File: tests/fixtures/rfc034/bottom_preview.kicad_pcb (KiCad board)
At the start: 2 copper layers, 75 x 58 mm, 16 parts, among them Q1 NPN_SOT23_BEC, Q2 NPN_SOT23_BEC, Q3 NPN_SOT23_BEC, Q4 NPN_SOT23_BEC, U1 W25Q128JV, U2 W25Q128JV, U3 W25Q128JV, U4 W25Q128JV

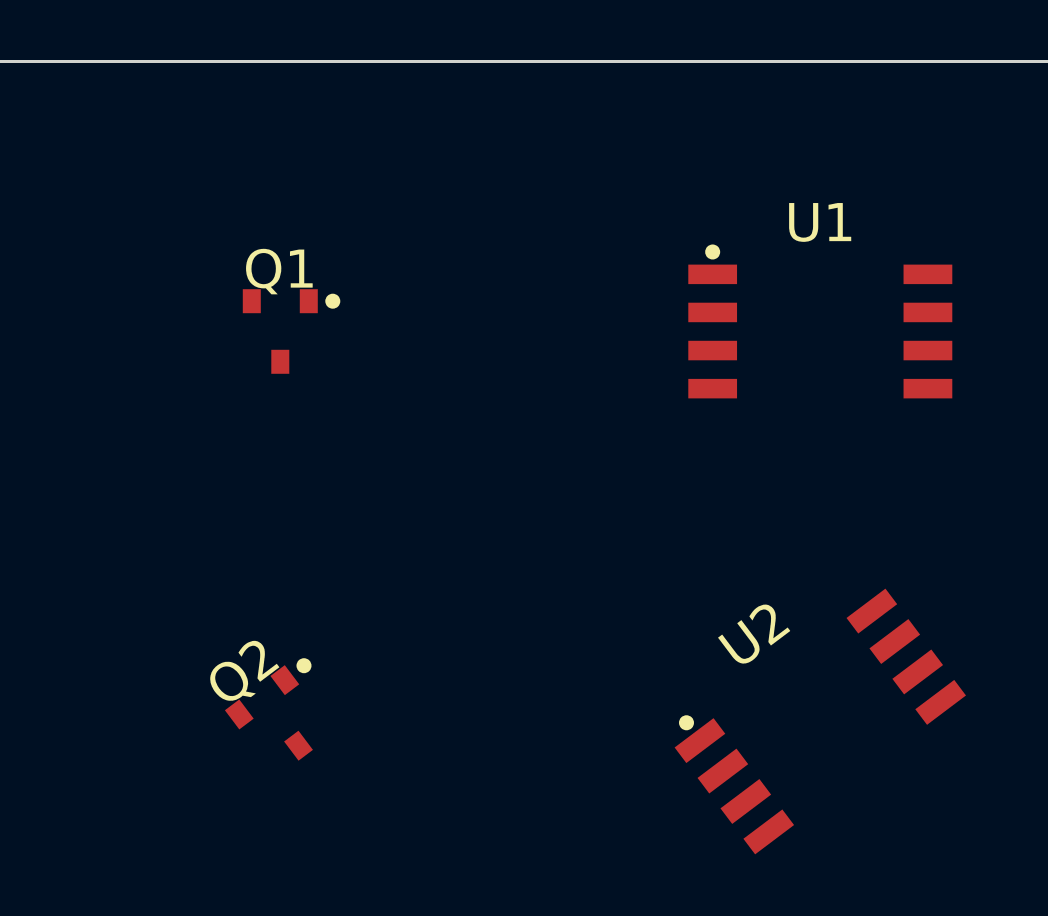
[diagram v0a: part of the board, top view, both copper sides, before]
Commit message: Move nine footprints onto the assembler's frame (library plan W3)
The C2 board 1 preview measured these footprints at a constant quarter
turn from the assembler's models, the same on every copy:

- transistor 0.2.0: FP_JSCJ_SOT23 by (0, 0, 90);
- soic 0.3.0: SOIC8P127X790X216N, TI_D0008A_4214825C,
  TSSOP24P65_TI_PW0024A, KICAD_SOIC_8_3_9X4_9MM_P1_27MM and
  KICAD_TSSOP_20_4_4X6_5MM_P0_65MM by (0, 0, 270);
- qfp 0.3.0: QFP50P900X900X160_48N, KICAD_LQFP_32_7X7MM_P0_8MM and
  KICAD_LQFP_48_7X7MM_P0_5MM by (0, 0, 270).

The hand-written ones are moved with tools/realign_footprint.py. The
generated ones are moved by gen_stm32_footprints.py from
tools/stm32_footprint_data/supplier_frames.json, which
tests/stm32_footprints.rs applies independently to the KiCad snapshot.

The change is breaking, so the three packages and every dependent
whose parts use a moved footprint take a minor version: can, flash,
@st/stm32, @ti/logic, @contrib/comparator, @wch/ch32 and
@gigadevice/gd32. @contrib/level-shifter only follows its pins and
takes a patch. Locks were refreshed with `cohdl update`. Package docs
list each delta and correct their orientation statements.

Consumers keep their copper. realign_place.py composed the examples'
and the bottom-preview fixture's placements with the deltas; the CAN
transceiver inside joint-motor-controller's subdesign was composed by
hand. KiCad compared every pad before and after (position, size,
shape, layers, orientation): 0 differences on all three examples, on
the fixture and on C2 board 1 (1124 pads, top, bottom, 0 and 37
degrees).

The fixture's supplier maps are now zero, and its CPL is still byte
for byte the assembler's aligned reference. The A6 generator fixture
follows the same change. The 11 frame rows for these footprints now
name the new versions with a zero mapping; `measured` keeps the
pre-move value. The SOT-23-5/6 parts keep per-part mappings: their
models differ by part on matching lands.

The examples' outputs are rebuilt, which a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
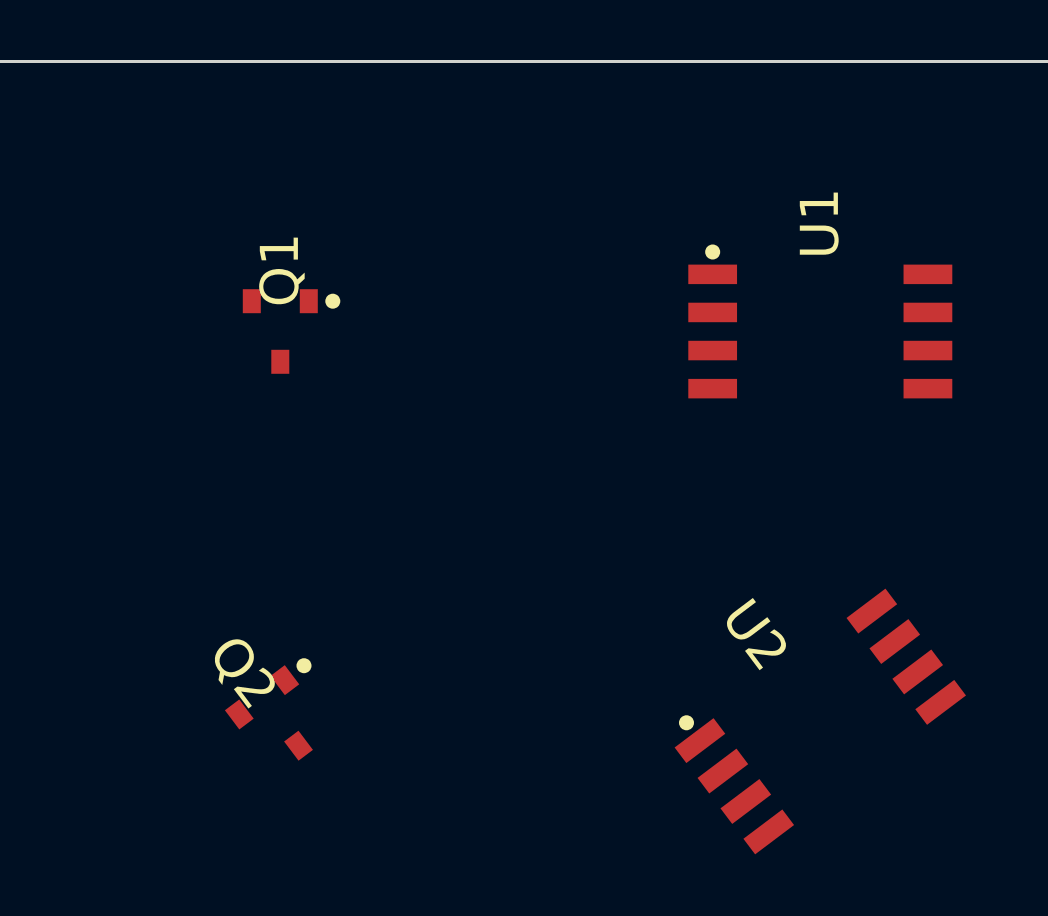
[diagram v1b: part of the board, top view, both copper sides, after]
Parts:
- turned Q1 to 90 degrees
- turned Q2 to 127 degrees
- turned Q3 to 90 degrees
- turned Q4 to 127 degrees
- turned U1 to -90 degrees
- turned U2 to -53 degrees
- turned U3 to -90 degrees
- turned U4 to -53 degrees
